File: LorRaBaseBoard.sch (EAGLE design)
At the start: 6 parts, among them J4 U.FL, X1 BU-SMA-H

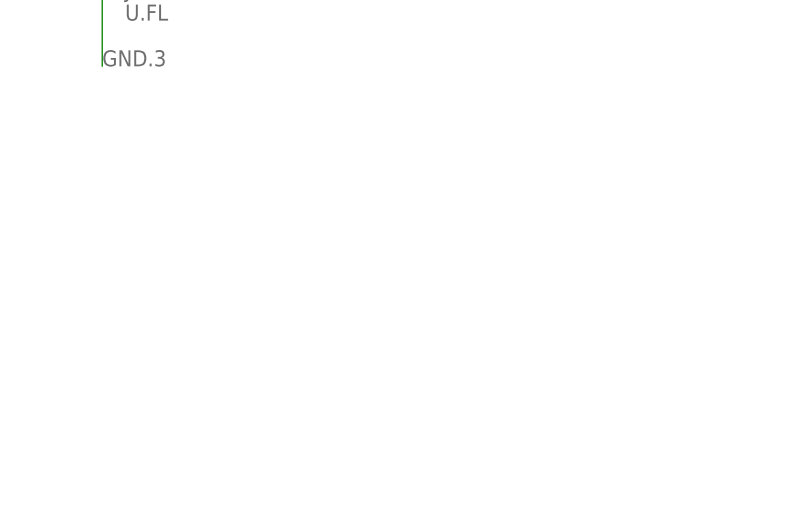
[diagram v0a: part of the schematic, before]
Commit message: Add Midnight Fog logos
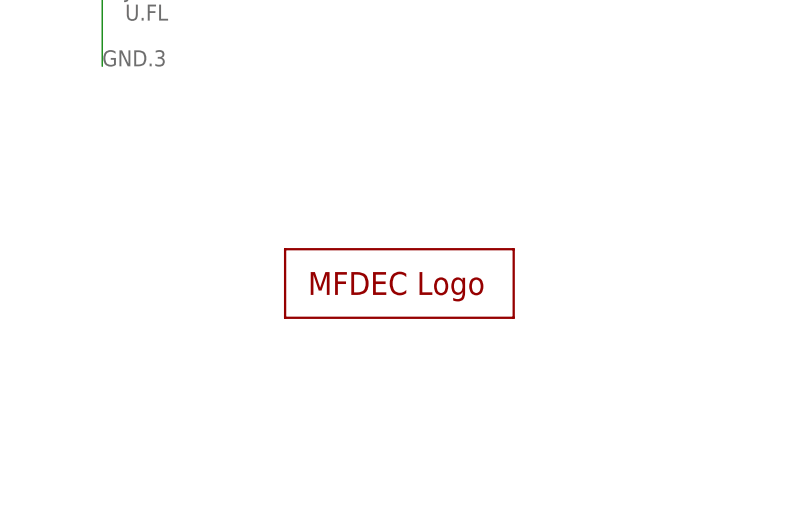
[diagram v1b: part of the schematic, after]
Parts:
- added LOGO1: MFDECLOGO_SQ_8MM, _my_logos:MFDECLOGO_SQ_8MM
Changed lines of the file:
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@@
 <part name="J4" library="SparkFun-Connectors" deviceset="U.FL2PIN" device="" value="U.FL"/>
 <part name="X1" library="con-coax" library_urn="urn:adsk.eagle:library:133" deviceset="BU-SMA-H" device="" package3d_urn="urn:adsk.eagle:package:6206/1"/>
+<part name="LOGO1" library="_my_logos" deviceset="MFDECLOGO" device="_SQ_8MM"/>
 </parts>
 <sheets>
@@
 <attribute name="NAME" x="106.68" y="69.342" size="1.778" layer="95"/>
 </instance>
+<instance part="LOGO1" gate="G$1" x="165.1" y="25.4" smashed="yes"/>
 </instances>
 <busses>

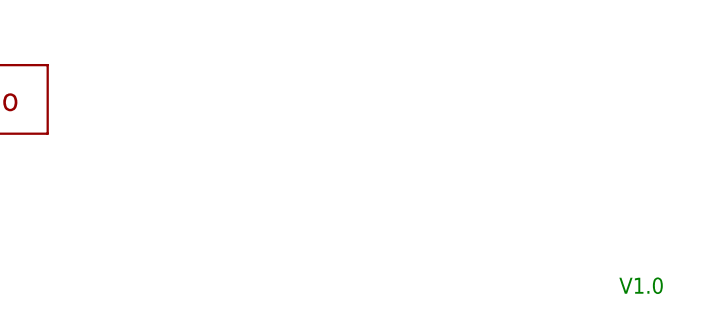
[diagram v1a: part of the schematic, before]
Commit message: Added board ids. Changed some visuals.
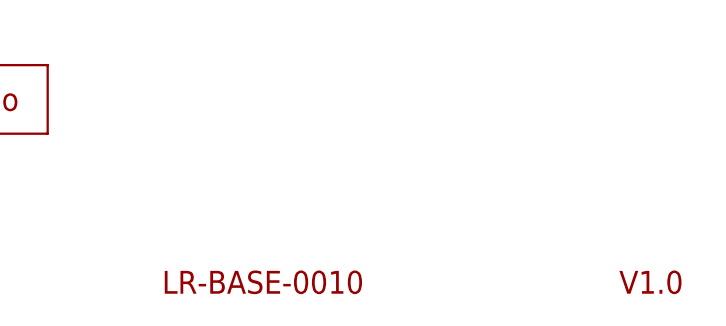
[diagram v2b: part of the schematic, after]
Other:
- note added: "LR-BASE-0010"
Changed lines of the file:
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@@
 <sheet>
 <plain>
-<text x="254" y="7.62" size="1.778" layer="91">V1.0</text>
+<text x="254" y="7.62" size="2.54" layer="94">V1.0</text>
+<text x="203.2" y="7.62" size="2.54" layer="94">LR-BASE-0010</text>
 </plain>
 <instances>

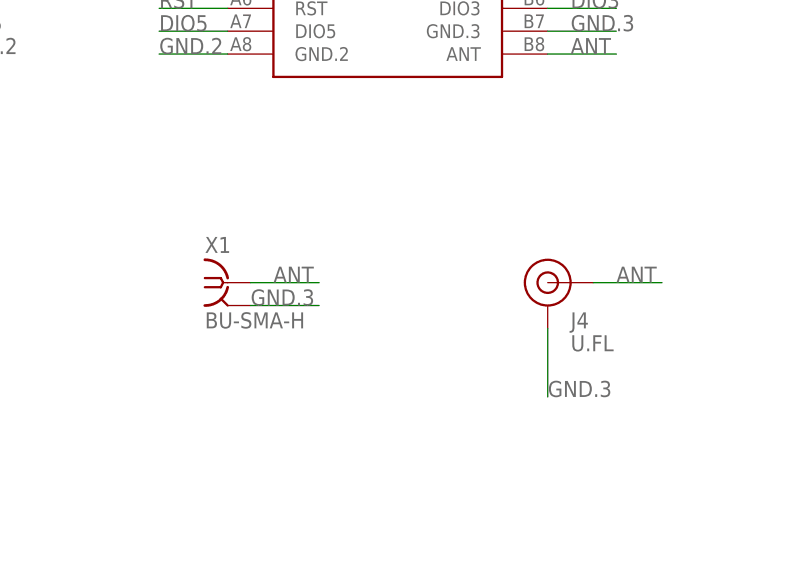
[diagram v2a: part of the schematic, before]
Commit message: Renamed antenna connectors.
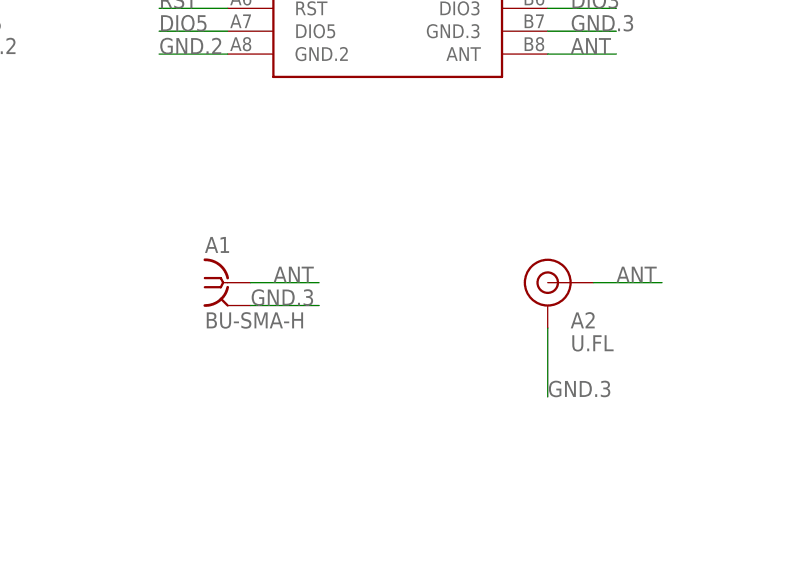
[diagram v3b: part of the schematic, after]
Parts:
- renumbered J4 to A2, X1 to A1
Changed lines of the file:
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@@
 <part name="J2" library="SparkFun-Connectors" deviceset="CONN_08" device="NO_SILK_FEMALE_PTH"/>
 <part name="J3" library="SparkFun-Connectors" deviceset="CONN_08" device="NO_SILK_FEMALE_PTH"/>
-<part name="J4" library="SparkFun-Connectors" deviceset="U.FL2PIN" device="" value="U.FL"/>
-<part name="X1" library="con-coax" library_urn="urn:adsk.eagle:library:133" deviceset="BU-SMA-H" device="" package3d_urn="urn:adsk.eagle:package:6206/1"/>
+<part name="A2" library="SparkFun-Connectors" deviceset="U.FL2PIN" device="" value="U.FL"/>
+<part name="A1" library="con-coax" library_urn="urn:adsk.eagle:library:133" deviceset="BU-SMA-H" device="" package3d_urn="urn:adsk.eagle:package:6206/1"/>
 <part name="LOGO1" library="_my_logos" deviceset="MFDECLOGO" device="_SQ_8MM"/>
 </parts>
@@
 <attribute name="NAME" x="215.9" y="112.268" size="1.778" layer="95" font="vector"/>
 </instance>
-<instance part="J4" gate="G$1" x="144.78" y="66.04" smashed="yes">
+<instance part="A2" gate="G$1" x="144.78" y="66.04" smashed="yes">
 <attribute name="NAME" x="147.32" y="60.96" size="1.778" layer="95"/>
 <attribute name="VALUE" x="147.32" y="58.42" size="1.778" layer="96"/>
 </instance>
-<instance part="X1" gate="G$1" x="109.22" y="66.04" smashed="yes">
+<instance part="A1" gate="G$1" x="109.22" y="66.04" smashed="yes">
 <attribute name="VALUE" x="106.68" y="60.96" size="1.778" layer="96"/>
 <attribute name="NAME" x="106.68" y="69.342" size="1.778" layer="95"/>
@@
 </segment>
 <segment>
-<pinref part="J4" gate="G$1" pin="GND"/>
+<pinref part="A2" gate="G$1" pin="GND"/>
 <wire x1="144.78" y1="60.96" x2="144.78" y2="53.34" width="0.1524" layer="91"/>
 <label x="144.78" y="53.34" size="1.778" layer="95"/>
 </segment>
 <segment>
-<pinref part="X1" gate="G$1" pin="2"/>
+<pinref part="A1" gate="G$1" pin="2"/>
 <wire x1="111.76" y1="63.5" x2="119.38" y2="63.5" width="0.1524" layer="91"/>
 <label x="111.76" y="63.5" size="1.778" layer="95"/>
@@
 </segment>
 <segment>
-<pinref part="J4" gate="G$1" pin="SIGNAL"/>
+<pinref part="A2" gate="G$1" pin="SIGNAL"/>
 <wire x1="149.86" y1="66.04" x2="157.48" y2="66.04" width="0.1524" layer="91"/>
 <label x="152.4" y="66.04" size="1.778" layer="95"/>
 </segment>
 <segment>
-<pinref part="X1" gate="G$1" pin="1"/>
+<pinref part="A1" gate="G$1" pin="1"/>
 <wire x1="111.76" y1="66.04" x2="119.38" y2="66.04" width="0.1524" layer="91"/>
 <label x="114.3" y="66.04" size="1.778" layer="95"/>
